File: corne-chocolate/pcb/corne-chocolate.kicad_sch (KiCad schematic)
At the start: 87 parts, among them J1 MJ-4PP-9, J2 OLED, J3 LED, P1 i2c-pin, P2 i2c-pin, SW1 SW_PUSH, SW10 SW_PUSH, SW11 SW_PUSH, SW12 SW_PUSH, SW13 SW_PUSH, SW14 SW_PUSH, SW15 SW_PUSH, SW16 SW_PUSH, SW17 SW_PUSH, SW18 SW_PUSH, SW19 SW_PUSH, SW2 SW_PUSH, SW20 SW_PUSH, SW21 SW_PUSH, SW3 SW_PUSH, SW4 SW_PUSH, SW5 SW_PUSH, SW6 SW_PUSH, SW7 SW_PUSH, SW8 SW_PUSH, SW9 SW_PUSH, U1 ProMicro

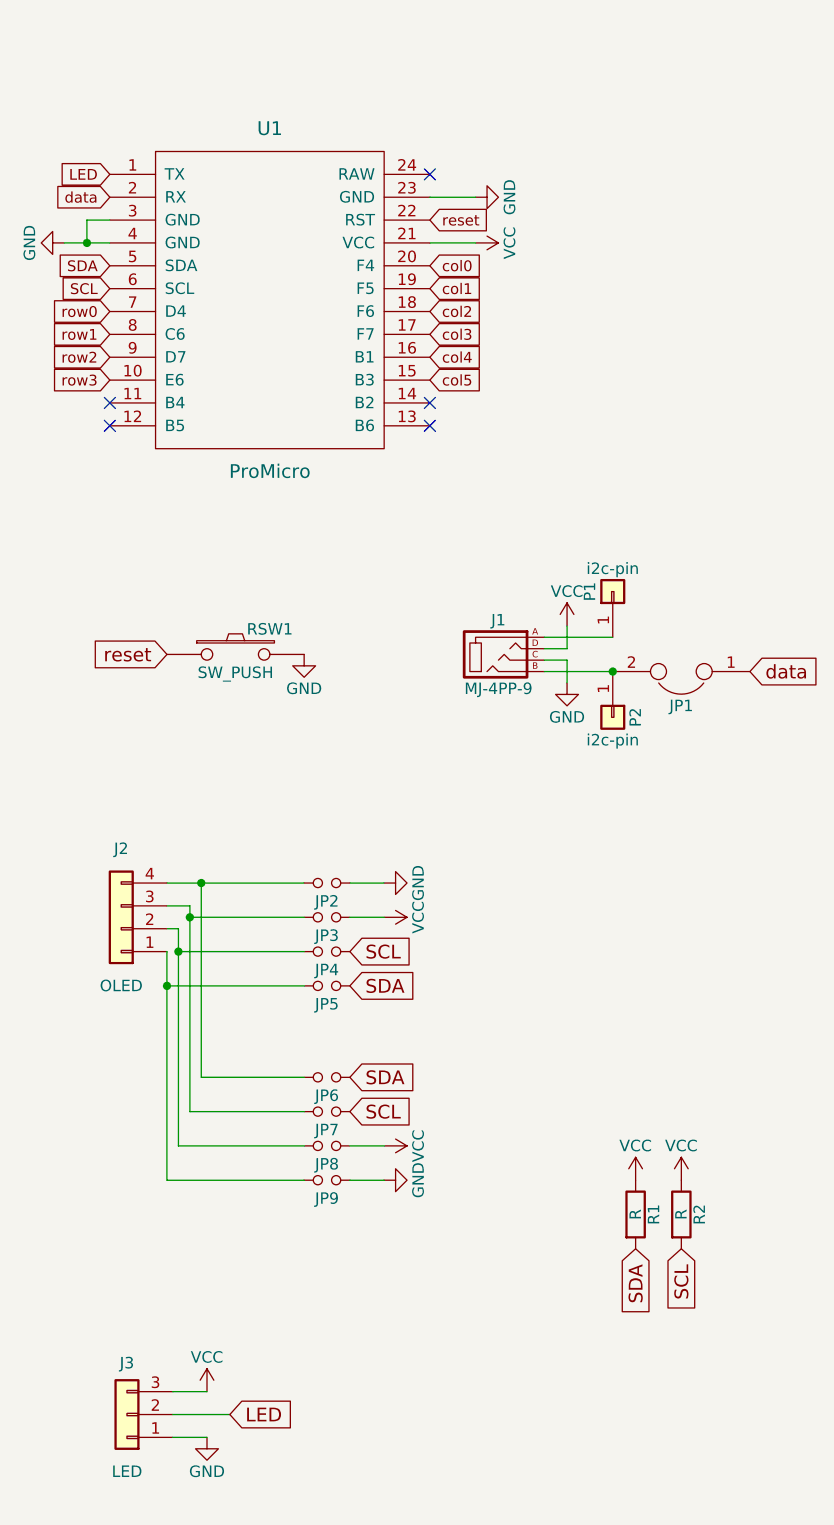
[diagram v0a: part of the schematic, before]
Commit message: merge foostan libraries. ERC checked.
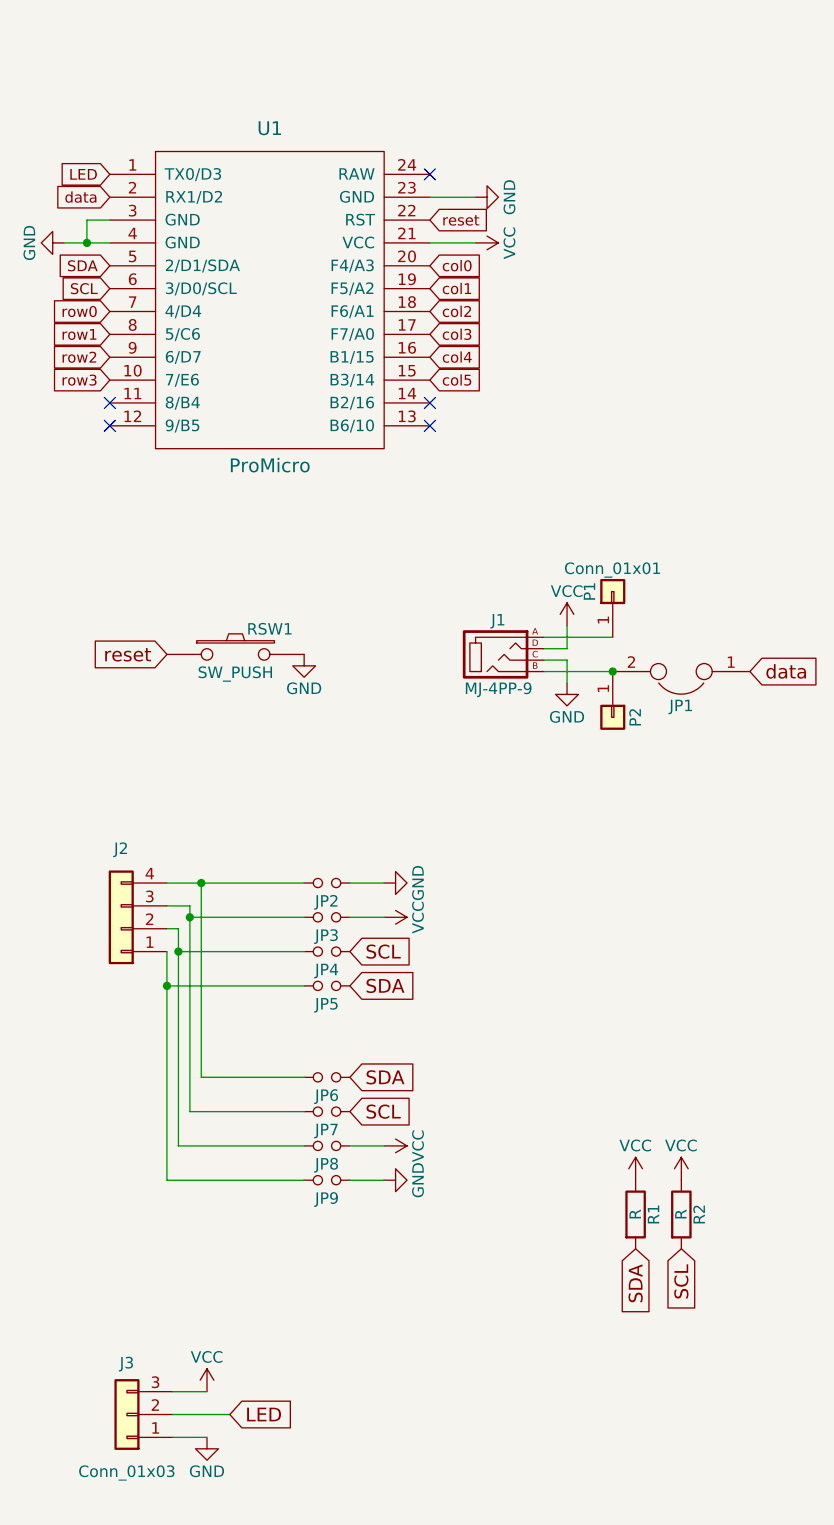
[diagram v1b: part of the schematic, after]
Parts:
- removed U1: ProMicro, kbd:ProMicro_v2, symbol corne-chocolate-rescue:ProMicro-kbd
- added U1: ProMicro, kbd:ProMicro_v2, symbol kbd:ProMicro
- D1, D10, D11, D12, D13, D14, D15, D16, D17, D18, D19, D2, D20, D21, D3, D4, D5, D6, D7, D8, D9: footprint kbd:D3_TH_SMD -> kbd:D3_SMD
- J1: symbol corne-chocolate-rescue:MJ-4PP-9-kbd -> kbd:MJ-4PP-9
- J2: value OLED -> Conn_01x04
- J3: value LED -> Conn_01x03
- JP1: value (none) -> Device:Jumper; symbol corne-chocolate-rescue:Jumper-Device -> kbd:Jumper-Device
- JP2, JP3, JP4, JP5, JP6, JP7, JP8, JP9: value (none) -> Device:Jumper_NO_Small; symbol corne-chocolate-rescue:Jumper_NO_Small-Device -> kbd:Jumper_NO_Small-Device
- L1, L10, L11, L12, L13, L14, L15, L16, L17, L18, L19, L2, L20, L21, L3, L4, L5, L6, L7, L8, L9: symbol corne-chocolate-rescue:SK6812MINI-kbd -> kbd:SK6812MINI
- L22, L23, L24, L25, L26, L27: footprint kbd:SK6812MINI_underglow -> kbd:SK6812MINI_underglow_rev; symbol corne-chocolate-rescue:SK6812MINI-kbd -> kbd:SK6812MINI
- P1, P2: value i2c-pin -> Conn_01x01
- RSW1: symbol corne-chocolate-rescue:SW_PUSH-kbd -> kbd:SW_PUSH
- SW1, SW10, SW11, SW12, SW13, SW14, SW15, SW16, SW17, SW18, SW19, SW2, SW20, SW3, SW4, SW5, SW6, SW7, SW8, SW9: footprint kbd:MX_ALPS_PG1350_noLed -> kbd:ChocV1_V2_Hotswap; symbol corne-chocolate-rescue:SW_PUSH-kbd -> kbd:SW_PUSH
- SW21: footprint kbd:MX_ALPS_PG1350_noLed_1.75u -> kbd:ChocV1_V2_Hotswap_1.5u; symbol corne-chocolate-rescue:SW_PUSH-kbd -> kbd:SW_PUSH
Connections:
- net GND: now also U1.23 (GND), U1.3 (GND), U1.4 (GND)
- net LED: now also U1.1 (TX0/D3)
- net SCL: now also U1.6 (3/D0/SCL)
- net SDA: now also U1.5 (2/D1/SDA)
- net VCC: now also U1.21 (VCC)
- net col0: now also U1.20 (F4/A3)
- net col1: now also U1.19 (F5/A2)
- net col2: now also U1.18 (F6/A1)
- net col3: now also U1.17 (F7/A0)
- net col4: now also U1.16 (B1/15)
- net col5: now also U1.15 (B3/14)
- net data: now also U1.2 (RX1/D2)
- net reset: now also U1.22 (RST)
- net row0: now also U1.7 (4/D4)
- net row1: now also U1.8 (5/C6)
- net row2: now also U1.9 (6/D7)
- net row3: now also U1.10 (7/E6)

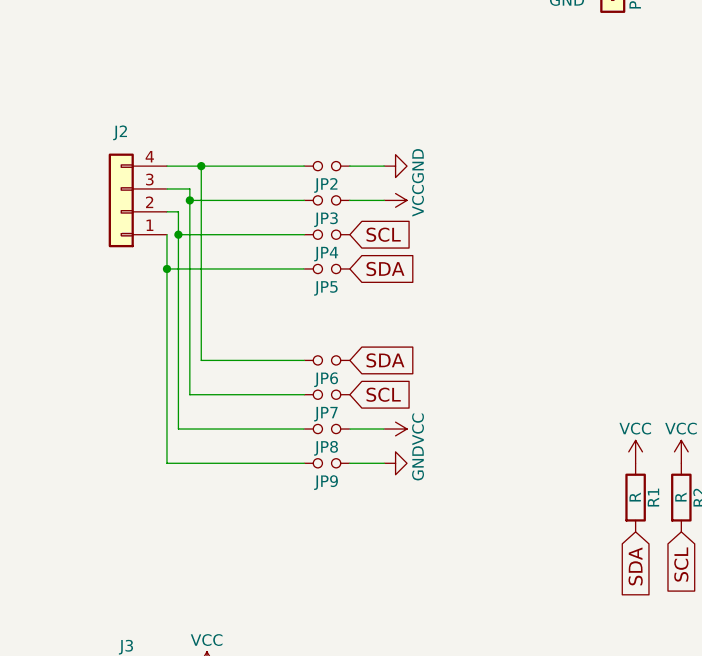
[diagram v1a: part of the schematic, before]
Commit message: starts non-reversable pcbs routing
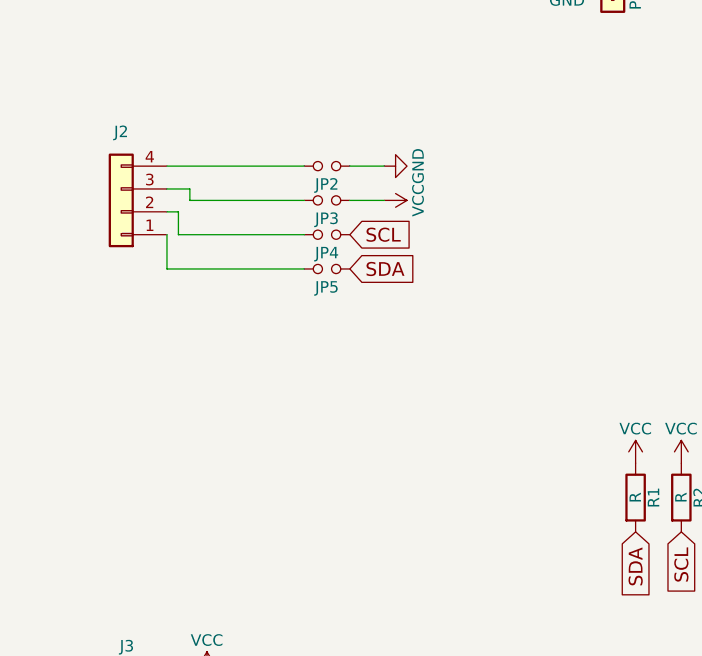
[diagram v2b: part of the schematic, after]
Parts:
- removed JP6, JP7, JP8, JP9: Device:Jumper_NO_Small, kbd:Jumper, symbol kbd:Jumper_NO_Small-Device
- J1: footprint kbd:MJ-4PP-9 -> kbd:MJ-4PP-9_1side
- J2: footprint kbd:OLED -> kbd:OLED_1side
- RSW1: footprint kbd:ResetSW -> kbd:ResetSW_1side
- U1: footprint kbd:ProMicro_v2 -> kbd:ProMicro_v2_1side

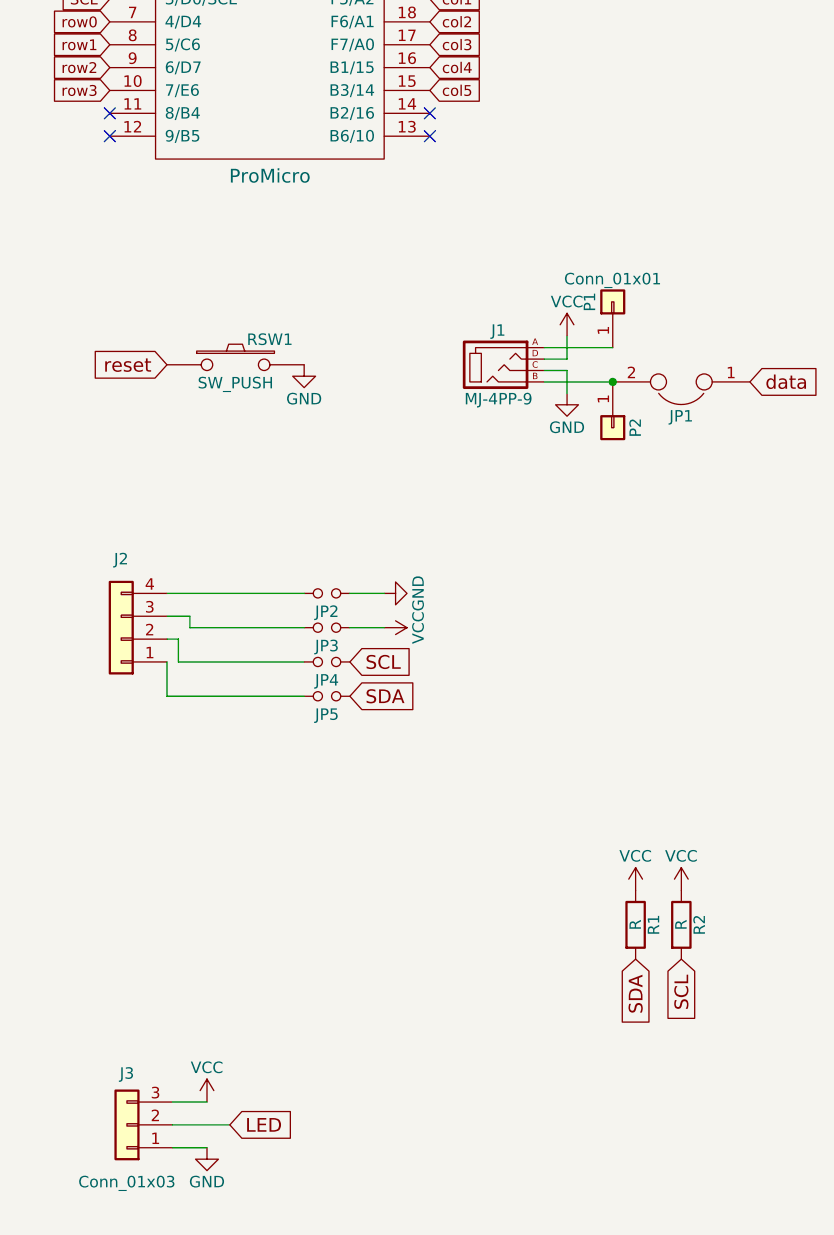
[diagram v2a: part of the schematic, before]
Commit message: removes all reversible routing
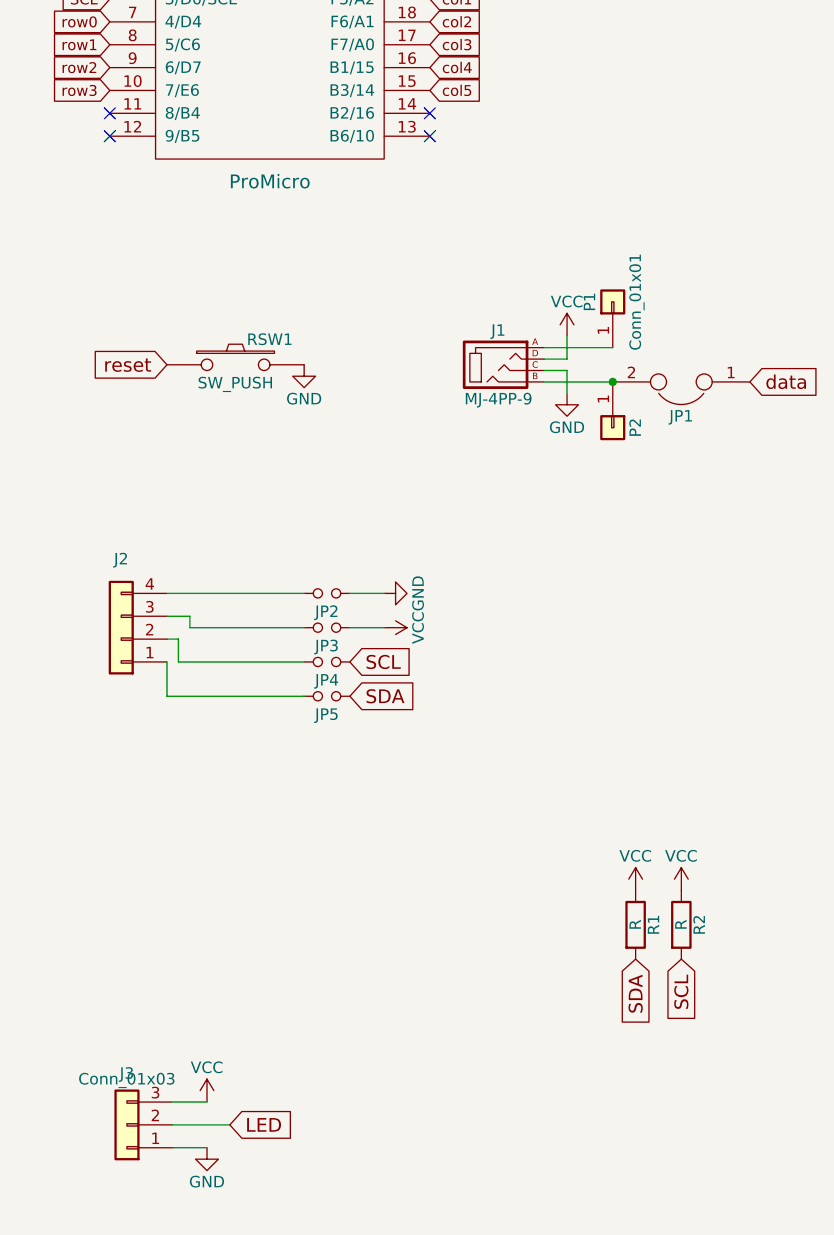
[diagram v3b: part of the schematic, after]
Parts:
- J3: footprint kbd:StripLED_rev -> kbd:StripLED_1side
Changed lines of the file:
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@@
       (effects (font (size 1.27 1.27)))
     )
-    (property "Value" "Conn_01x04" (at 29.21 120.65 0)
+    (property "Value" "Conn_01x04" (at 29.21 106.68 0)
       (effects (font (size 1.27 1.27)) hide)
     )
@@
       (effects (font (size 1.27 1.27)))
     )
-    (property "Value" "Conn_01x03" (at 29.845 174.625 0)
-      (effects (font (size 1.27 1.27)))
-    )
-    (property "Footprint" "kbd:StripLED_rev" (at 29.845 168.275 0)
+    (property "Value" "Conn_01x03" (at 29.845 163.195 0)
+      (effects (font (size 1.27 1.27)))
+    )
+    (property "Footprint" "kbd:StripLED_1side" (at 29.845 168.275 0)
       (effects (font (size 1.27 1.27)) hide)
     )
@@
       (effects (font (size 1.27 1.27)))
     )
-    (property "Value" "Conn_01x01" (at 83.82 93.345 90)
+    (property "Value" "Conn_01x01" (at 81.28 90.805 0)
       (effects (font (size 1.27 1.27)) hide)
     )
@@
       (effects (font (size 1.27 1.27)))
     )
-    (property "Value" "Conn_01x01" (at 83.82 74.295 90)
+    (property "Value" "Conn_01x01" (at 86.36 76.835 0)
       (effects (font (size 1.27 1.27)))
     )
@@
       (effects (font (size 1.524 1.524)))
     )
-    (property "Value" "ProMicro" (at 45.72 62.865 0)
+    (property "Value" "ProMicro" (at 45.72 63.5 0)
       (effects (font (size 1.524 1.524)))
     )

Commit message: starts re-routing. switch to a 3x5 kbd
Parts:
- removed D1, D13, D7: D, kbd:D3_SMD, symbol Device:D
- removed L1, L13, L7: SK6812MINI, kbd:SK6812MINI_rev, symbol kbd:SK6812MINI
- removed SW1, SW13, SW7: SW_PUSH, kbd:ChocV1_V2_Hotswap, symbol kbd:SW_PUSH
- JP1: footprint kbd:JPC2 -> kbd:Jumper
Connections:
- net GND: now also JP2.2; no longer JP2.1
- net data: now also J1.B, JP1.2, P2.1 (Pin_1)
- net at J2.4 (Pin_4): now also JP2.1; no longer JP2.2
- net col0: no longer names the net of U1.20 (F4/A3)
- no-connect marks 6 -> 7
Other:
- moved on the sheet: J1, J2, J3, JP3, JP4, JP5, L10, L11, L12, L14, L15, L16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
